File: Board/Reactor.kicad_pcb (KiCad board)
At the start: 2 copper layers, 72.4 x 77.1 mm, 27 parts, among them P1 CONN_02X13, P2 USER_PORT, P3 CONN_01X13, P4 CONN_01X02, P5 USB_OTG, P6 DEBUG, P7 CONN_01X10, P8 CONN_01X02, P9 CONN_01X10, U2 PCF8574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

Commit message: Testing of new board
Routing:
- net /PA1: track 87.6 -> 83.7 mm
- net /PA16: track 102.8 -> 100.9 mm
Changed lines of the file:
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@@
     (thickness 1.6)
     (drawings 9602)
-    (tracks 557)
+    (tracks 554)
     (zones 0)
     (modules 27)
@@
   (segment (start 162.0266 115.9764) (end 156.7815 115.9764) (width 0.25) (layer F.Cu) (net 63))
   (segment (start 163.1569 117.221) (end 163.1569 117.9449) (width 0.25) (layer B.Cu) (net 63))
-  (segment (start 163.1569 117.9449) (end 162.4838 118.618) (width 0.25) (layer B.Cu) (net 63))
-  (segment (start 162.4838 118.618) (end 159.4739 118.618) (width 0.25) (layer B.Cu) (net 63))
   (segment (start 155.5369 117.221) (end 155.5369 120.0531) (width 0.25) (layer B.Cu) (net 63))
   (segment (start 155.5369 120.0531) (end 152.4 123.19) (width 0.25) (layer B.Cu) (net 63))
@@
   (segment (start 128.26576 89.27) (end 128.13792 89.39784) (width 0.25) (layer F.Cu) (net 65))
   (segment (start 124.48216 89.39784) (end 124.39 89.49) (width 0.25) (layer F.Cu) (net 65))
-  (segment (start 159.4739 118.618) (end 158.0769 117.221) (width 0.25) (layer B.Cu) (net 65))
   (segment (start 165.1 123.19) (end 165.1 121.67) (width 0.25) (layer F.Cu) (net 65))
   (segment (start 158.0769 117.221) (end 157.741 117.221) (width 0.25) (layer B.Cu) (net 65))

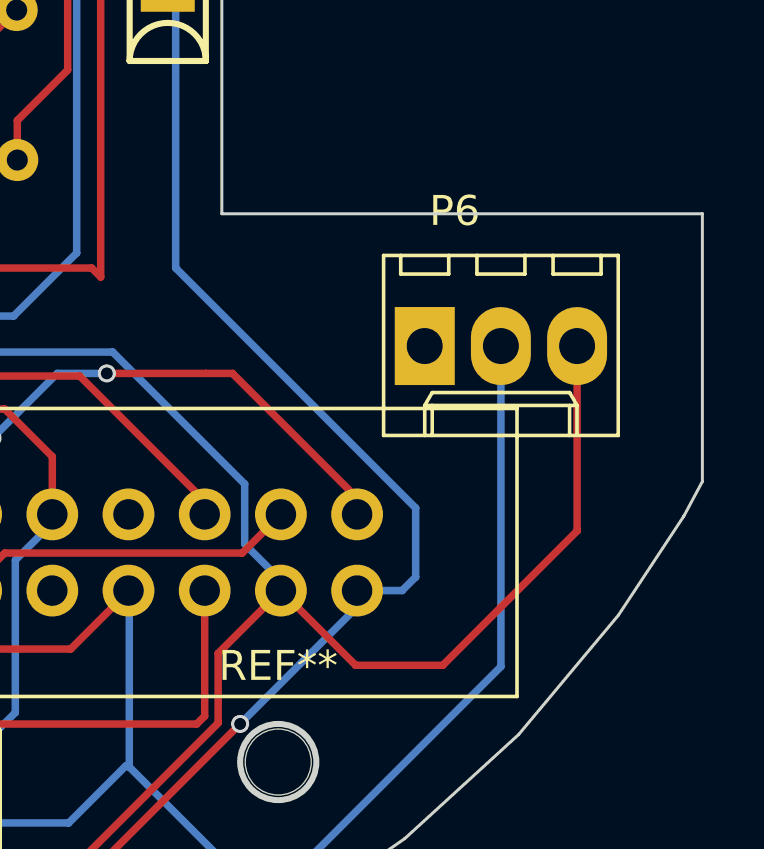
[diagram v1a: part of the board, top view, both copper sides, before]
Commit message: Fixed bad tracks
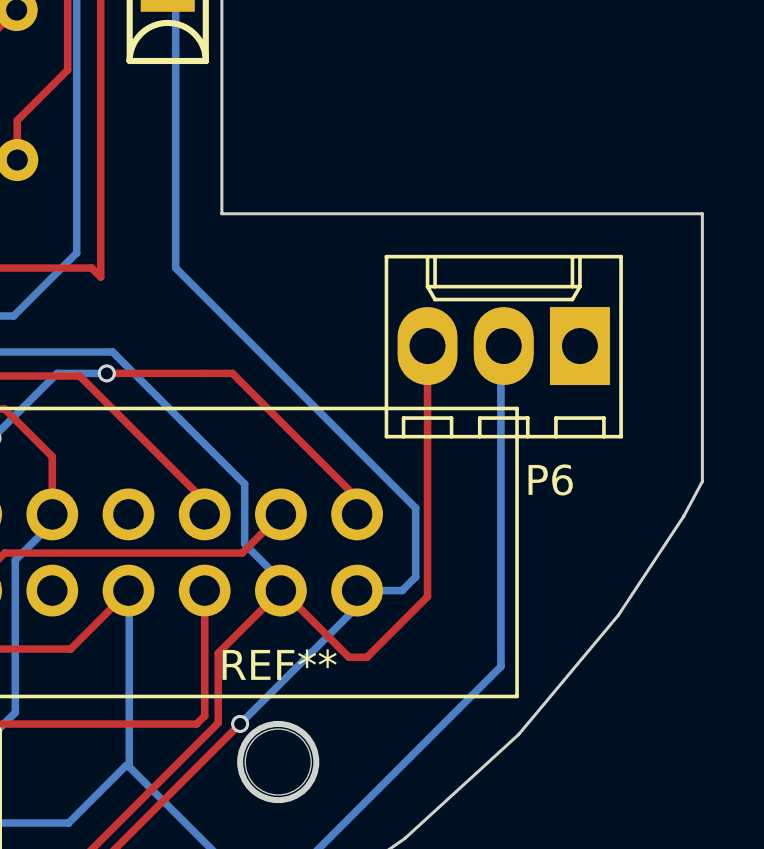
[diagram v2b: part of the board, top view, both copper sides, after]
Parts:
- moved P6 5.18 mm to (188.4, 109.1), turned to 180 degrees
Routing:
- net /PA14: track 123.3 -> 119.4 mm
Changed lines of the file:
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@@
     (thickness 1.6)
     (drawings 9602)
-    (tracks 554)
+    (tracks 555)
     (zones 0)
     (modules 27)
@@
   )
   (module Connectors_Molex:Molex_KK-6410-03_03x2.54mm_Straight (layer F.Cu)
-    (at 183.19 109.07)
+    (at 188.365 109.07 180)
     (descr "Connector Headers with Friction Lock, 22-27-2031, http://www.molex.com/pdm_docs/sd/022272021_sd.pdf")
     (tags "connector molex kk_6410 22-27-2031")
-    (fp_text reference P6 (at 1 -4.5) (layer F.SilkS)
+    (fp_text reference P6 (at 1 -4.5 180) (layer F.SilkS)
       (effects (font (size 1 1) (thickness 0.15)))
     )
-    (fp_text value DEBUG (at 2.54 4.5) (layer F.Fab)
+    (fp_text value DEBUG (at 2.54 4.5 180) (layer F.Fab)
       (effects (font (size 1 1) (thickness 0.15)))
     )
@@
     (fp_line (start 7 -3.55) (end 7 3.5) (layer F.CrtYd) (width 0.05))
     (fp_line (start 7 3.5) (end -1.9 3.5) (layer F.CrtYd) (width 0.05))
-    (pad 1 thru_hole rect (at 0 0) (size 2 2.6) (drill 1.2) (layers *.Cu *.Mask)
+    (pad 1 thru_hole rect (at 0 0 180) (size 2 2.6) (drill 1.2) (layers *.Cu *.Mask)
       (net 21 "Net-(P6-Pad1)"))
-    (pad 2 thru_hole oval (at 2.54 0) (size 2 2.6) (drill 1.2) (layers *.Cu *.Mask)
+    (pad 2 thru_hole oval (at 2.54 0 180) (size 2 2.6) (drill 1.2) (layers *.Cu *.Mask)
       (net 69 /PA15))
-    (pad 3 thru_hole oval (at 5.08 0) (size 2 2.6) (drill 1.2) (layers *.Cu *.Mask)
+    (pad 3 thru_hole oval (at 5.08 0 180) (size 2 2.6) (drill 1.2) (layers *.Cu *.Mask)
       (net 70 /PA14))
   )
@@
   (segment (start 173.3423 123.1011) (end 173.3423 117.2464) (width 0.25) (layer B.Cu) (net 69))
   (segment (start 173.3423 117.2464) (end 173.3169 117.221) (width 0.25) (layer B.Cu) (net 69))
-  (segment (start 185.73 109.07) (end 185.73 119.7558) (width 0.25) (layer B.Cu) (net 69))
   (segment (start 176.657 126.4158) (end 173.3423 123.1011) (width 0.25) (layer B.Cu) (net 69))
   (segment (start 173.3423 123.1011) (end 173.3112 123.07) (width 0.25) (layer B.Cu) (net 69))
   (segment (start 179.07 126.4158) (end 176.657 126.4158) (width 0.25) (layer B.Cu) (net 69))
-  (segment (start 185.73 119.7558) (end 179.07 126.4158) (width 0.25) (layer B.Cu) (net 69))
   (segment (start 173.3112 123.07) (end 173.221 123.07) (width 0.25) (layer B.Cu) (net 69))
   (segment (start 164.338 124.968) (end 162.56 123.19) (width 0.25) (layer B.Cu) (net 69))
@@
   (segment (start 162.79 110.77) (end 162.79 108.67) (width 0.25) (layer B.Cu) (net 69))
   (segment (start 164.39 112.37) (end 162.79 110.77) (width 0.25) (layer B.Cu) (net 69))
+  (segment (start 185.73 109.07) (end 185.73 119.7558) (width 0.25) (layer B.Cu) (net 69))
+  (segment (start 185.73 119.7558) (end 179.07 126.4158) (width 0.25) (layer B.Cu) (net 69))
+  (segment (start 178.3969 117.221) (end 178.441 117.221) (width 0.25) (layer F.Cu) (net 70) (status C00000))
+  (segment (start 178.441 117.221) (end 180.665 119.445) (width 0.25) (layer F.Cu) (net 70) (status 400000))
+  (segment (start 183.285 117.425) (end 183.285 109.07) (width 0.25) (layer F.Cu) (net 70) (status 800000))
+  (segment (start 181.265 119.445) (end 183.285 117.425) (width 0.25) (layer F.Cu) (net 70))
+  (segment (start 180.665 119.445) (end 181.265 119.445) (width 0.25) (layer F.Cu) (net 70))
   (segment (start 149.02966 104.60966) (end 146.02966 104.60966) (width 0.25) (layer B.Cu) (net 70))
   (segment (start 145.89 104.47) (end 143.99 102.57) (width 0.25) (layer B.Cu) (net 70))
@@
   (segment (start 128.23511 94.26381) (end 128.0414 94.45752) (width 0.25) (layer F.Cu) (net 70))
   (segment (start 124.50248 94.45752) (end 124.39 94.57) (width 0.25) (layer F.Cu) (net 70))
-  (segment (start 188.27 109.07) (end 188.27 115.2346) (width 0.25) (layer F.Cu) (net 70))
-  (segment (start 180.8861 119.7102) (end 178.3969 117.221) (width 0.25) (layer F.Cu) (net 70))
-  (segment (start 183.7944 119.7102) (end 180.8861 119.7102) (width 0.25) (layer F.Cu) (net 70))
-  (segment (start 188.27 115.2346) (end 183.7944 119.7102) (width 0.25) (layer F.Cu) (net 70))
   (segment (start 160.02 123.19) (end 160.02 123.317) (width 0.25) (layer F.Cu) (net 70))
   (segment (start 160.02 123.317) (end 162.687 125.984) (width 0.25) (layer F.Cu) (net 70))
